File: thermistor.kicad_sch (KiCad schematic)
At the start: 2 parts, among them Q13 AO3400A

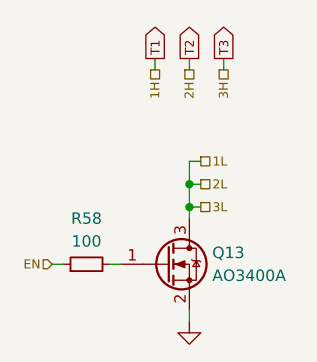
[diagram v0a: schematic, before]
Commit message: schematic: Reorder pages
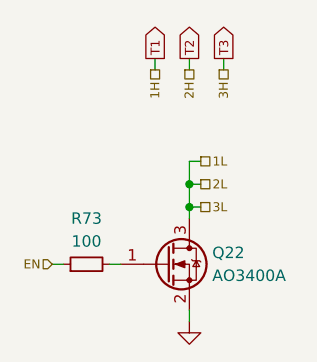
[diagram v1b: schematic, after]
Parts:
- renumbered Q13 to Q22, R58 to R73
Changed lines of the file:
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@@
 		(dnp no)
 		(fields_autoplaced yes)
-		(property "Reference" "R58"
+		(property "Reference" "R73"
 			(at 66.04 69.85 90)
 			(effects
@@
 		(on_board yes)
 		(dnp no)
-		(property "Reference" "Q13"
+		(property "Reference" "Q22"
 			(at 80.01 73.66 0)
 			(effects
@@
 		(dnp no)
 		(fields_autoplaced yes)
-		(property "Reference" "#PWR035"
+		(property "Reference" "#PWR063"
 			(at 77.47 87.63 0)
 			(effects

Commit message: schematic: Cleanup
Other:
- company: (none) -> York Formula Student
- title: (none) -> Battery Management System
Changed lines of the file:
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@@
 	(generator_version "8.0")
 	(paper "A4")
+	(title_block
+		(title "Battery Management System")
+		(date "2025-02-08")
+		(rev "1")
+		(company "York Formula Student")
+	)
 	(junction
 		(at 77.47 68.58)

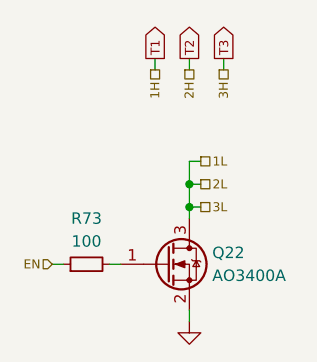
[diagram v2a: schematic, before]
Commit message: schematic: Re-annotate designators
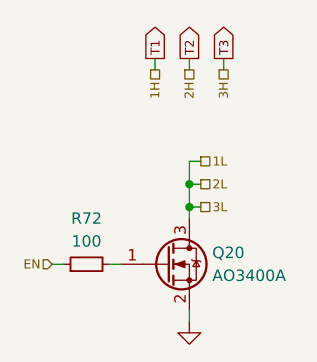
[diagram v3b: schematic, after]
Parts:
- renumbered Q22 to Q20, R73 to R72
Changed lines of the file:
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@@
 		(dnp no)
 		(fields_autoplaced yes)
-		(property "Reference" "R73"
+		(property "Reference" "R72"
 			(at 66.04 69.85 90)
 			(effects
@@
 			(project "bms"
 				(path "/ae4a7653-8e6d-4e05-b144-1e5e3b2092b7/22f96080-372f-4edc-adbb-6967cdfa7222/0d2d7204-129d-421c-bcc5-b71bb72cba95"
+					(reference "R72")
+					(unit 1)
+				)
+				(path "/ae4a7653-8e6d-4e05-b144-1e5e3b2092b7/22f96080-372f-4edc-adbb-6967cdfa7222/29137b06-2a79-41e8-a20a-ffb792999e98"
+					(reference "R74")
+					(unit 1)
+				)
+				(path "/ae4a7653-8e6d-4e05-b144-1e5e3b2092b7/22f96080-372f-4edc-adbb-6967cdfa7222/79ecc304-8e18-444c-9a27-bb0ae7f09105"
+					(reference "R71")
+					(unit 1)
+				)
+				(path "/ae4a7653-8e6d-4e05-b144-1e5e3b2092b7/22f96080-372f-4edc-adbb-6967cdfa7222/7d586639-e148-4a8a-9ad9-620c1fe14641"
+					(reference "R69")
+					(unit 1)
+				)
+				(path "/ae4a7653-8e6d-4e05-b144-1e5e3b2092b7/22f96080-372f-4edc-adbb-6967cdfa7222/8f54f16c-7967-437d-a988-e231275c63ab"
+					(reference "R66")
+					(unit 1)
+				)
+				(path "/ae4a7653-8e6d-4e05-b144-1e5e3b2092b7/22f96080-372f-4edc-adbb-6967cdfa7222/9c1ee688-8492-4d78-a310-31dcbd30b38f"
+					(reference "R68")
+					(unit 1)
+				)
+				(path "/ae4a7653-8e6d-4e05-b144-1e5e3b2092b7/22f96080-372f-4edc-adbb-6967cdfa7222/bb249f9a-39ea-44a6-9a0b-74cb85e10ca5"
+					(reference "R75")
+					(unit 1)
+				)
+				(path "/ae4a7653-8e6d-4e05-b144-1e5e3b2092b7/22f96080-372f-4edc-adbb-6967cdfa7222/efd357bc-4550-47fb-96bd-8f3dacb5f594"
 					(reference "R73")
 					(unit 1)
 				)
-				(path "/ae4a7653-8e6d-4e05-b144-1e5e3b2092b7/22f96080-372f-4edc-adbb-6967cdfa7222/29137b06-2a79-41e8-a20a-ffb792999e98"
-					(reference "R66")
-					(unit 1)
-				)
-				(path "/ae4a7653-8e6d-4e05-b144-1e5e3b2092b7/22f96080-372f-4edc-adbb-6967cdfa7222/79ecc304-8e18-444c-9a27-bb0ae7f09105"
-					(reference "R74")
-					(unit 1)
-				)
-				(path "/ae4a7653-8e6d-4e05-b144-1e5e3b2092b7/22f96080-372f-4edc-adbb-6967cdfa7222/7d586639-e148-4a8a-9ad9-620c1fe14641"
-					(reference "R68")
-					(unit 1)
-				)
-				(path "/ae4a7653-8e6d-4e05-b144-1e5e3b2092b7/22f96080-372f-4edc-adbb-6967cdfa7222/8f54f16c-7967-437d-a988-e231275c63ab"
-					(reference "R71")
-					(unit 1)
-				)
-				(path "/ae4a7653-8e6d-4e05-b144-1e5e3b2092b7/22f96080-372f-4edc-adbb-6967cdfa7222/9c1ee688-8492-4d78-a310-31dcbd30b38f"
-					(reference "R69")
-					(unit 1)
-				)
-				(path "/ae4a7653-8e6d-4e05-b144-1e5e3b2092b7/22f96080-372f-4edc-adbb-6967cdfa7222/bb249f9a-39ea-44a6-9a0b-74cb85e10ca5"
-					(reference "R63")
-					(unit 1)
-				)
-				(path "/ae4a7653-8e6d-4e05-b144-1e5e3b2092b7/22f96080-372f-4edc-adbb-6967cdfa7222/efd357bc-4550-47fb-96bd-8f3dacb5f594"
-					(reference "R72")
-					(unit 1)
-				)
 				(path "/ae4a7653-8e6d-4e05-b144-1e5e3b2092b7/22f96080-372f-4edc-adbb-6967cdfa7222/f122550a-f09a-4f05-9f89-cb0637def957"
-					(reference "R58")
+					(reference "R65")
 					(unit 1)
 				)
 				(path "/ae4a7653-8e6d-4e05-b144-1e5e3b2092b7/22f96080-372f-4edc-adbb-6967cdfa7222/fa4bad2a-a064-460b-8083-ff08c7505cb9"
+					(reference "R70")
+					(unit 1)
+				)
+				(path "/ae4a7653-8e6d-4e05-b144-1e5e3b2092b7/22f96080-372f-4edc-adbb-6967cdfa7222/fa95d462-4de0-4934-af70-5f0e8f1d034c"
 					(reference "R67")
-					(unit 1)
-				)
-				(path "/ae4a7653-8e6d-4e05-b144-1e5e3b2092b7/22f96080-372f-4edc-adbb-6967cdfa7222/fa95d462-4de0-4934-af70-5f0e8f1d034c"
-					(reference "R70")
 					(unit 1)
 				)
@@
 		(on_board yes)
 		(dnp no)
-		(property "Reference" "Q22"
+		(property "Reference" "Q20"
 			(at 80.01 73.66 0)
 			(effects
@@
 			(project "bms"
 				(path "/ae4a7653-8e6d-4e05-b144-1e5e3b2092b7/22f96080-372f-4edc-adbb-6967cdfa7222/0d2d7204-129d-421c-bcc5-b71bb72cba95"
+					(reference "Q20")
+					(unit 1)
+				)
+				(path "/ae4a7653-8e6d-4e05-b144-1e5e3b2092b7/22f96080-372f-4edc-adbb-6967cdfa7222/29137b06-2a79-41e8-a20a-ffb792999e98"
 					(reference "Q22")
 					(unit 1)
 				)
-				(path "/ae4a7653-8e6d-4e05-b144-1e5e3b2092b7/22f96080-372f-4edc-adbb-6967cdfa7222/29137b06-2a79-41e8-a20a-ffb792999e98"
-					(reference "Q15")
-					(unit 1)
-				)
 				(path "/ae4a7653-8e6d-4e05-b144-1e5e3b2092b7/22f96080-372f-4edc-adbb-6967cdfa7222/79ecc304-8e18-444c-9a27-bb0ae7f09105"
-					(reference "Q23")
+					(reference "Q19")
 					(unit 1)
 				)
@@
 				)
 				(path "/ae4a7653-8e6d-4e05-b144-1e5e3b2092b7/22f96080-372f-4edc-adbb-6967cdfa7222/8f54f16c-7967-437d-a988-e231275c63ab"
-					(reference "Q20")
+					(reference "Q14")
 					(unit 1)
 				)
 				(path "/ae4a7653-8e6d-4e05-b144-1e5e3b2092b7/22f96080-372f-4edc-adbb-6967cdfa7222/9c1ee688-8492-4d78-a310-31dcbd30b38f"
-					(reference "Q18")
+					(reference "Q16")
 					(unit 1)
 				)
 				(path "/ae4a7653-8e6d-4e05-b144-1e5e3b2092b7/22f96080-372f-4edc-adbb-6967cdfa7222/bb249f9a-39ea-44a6-9a0b-74cb85e10ca5"
-					(reference "Q14")
+					(reference "Q23")
 					(unit 1)
 				)
@@
 				)
 				(path "/ae4a7653-8e6d-4e05-b144-1e5e3b2092b7/22f96080-372f-4edc-adbb-6967cdfa7222/fa4bad2a-a064-460b-8083-ff08c7505cb9"
-					(reference "Q16")
+					(reference "Q18")
 					(unit 1)
 				)
 				(path "/ae4a7653-8e6d-4e05-b144-1e5e3b2092b7/22f96080-372f-4edc-adbb-6967cdfa7222/fa95d462-4de0-4934-af70-5f0e8f1d034c"
-					(reference "Q19")
+					(reference "Q15")
 					(unit 1)
 				)
@@
 		(dnp no)
 		(fields_autoplaced yes)
-		(property "Reference" "#PWR063"
+		(property "Reference" "#PWR064"
 			(at 77.47 87.63 0)
 			(effects
@@
 			(project "bms"
 				(path "/ae4a7653-8e6d-4e05-b144-1e5e3b2092b7/22f96080-372f-4edc-adbb-6967cdfa7222/0d2d7204-129d-421c-bcc5-b71bb72cba95"
+					(reference "#PWR064")
+					(unit 1)
+				)
+				(path "/ae4a7653-8e6d-4e05-b144-1e5e3b2092b7/22f96080-372f-4edc-adbb-6967cdfa7222/29137b06-2a79-41e8-a20a-ffb792999e98"
+					(reference "#PWR066")
+					(unit 1)
+				)
+				(path "/ae4a7653-8e6d-4e05-b144-1e5e3b2092b7/22f96080-372f-4edc-adbb-6967cdfa7222/79ecc304-8e18-444c-9a27-bb0ae7f09105"
 					(reference "#PWR063")
 					(unit 1)
 				)
-				(path "/ae4a7653-8e6d-4e05-b144-1e5e3b2092b7/22f96080-372f-4edc-adbb-6967cdfa7222/29137b06-2a79-41e8-a20a-ffb792999e98"
-					(reference "#PWR056")
-					(unit 1)
-				)
-				(path "/ae4a7653-8e6d-4e05-b144-1e5e3b2092b7/22f96080-372f-4edc-adbb-6967cdfa7222/79ecc304-8e18-444c-9a27-bb0ae7f09105"
-					(reference "#PWR064")
-					(unit 1)
-				)
 				(path "/ae4a7653-8e6d-4e05-b144-1e5e3b2092b7/22f96080-372f-4edc-adbb-6967cdfa7222/7d586639-e148-4a8a-9ad9-620c1fe14641"
+					(reference "#PWR061")
+					(unit 1)
+				)
+				(path "/ae4a7653-8e6d-4e05-b144-1e5e3b2092b7/22f96080-372f-4edc-adbb-6967cdfa7222/8f54f16c-7967-437d-a988-e231275c63ab"
 					(reference "#PWR058")
 					(unit 1)
 				)
-				(path "/ae4a7653-8e6d-4e05-b144-1e5e3b2092b7/22f96080-372f-4edc-adbb-6967cdfa7222/8f54f16c-7967-437d-a988-e231275c63ab"
-					(reference "#PWR061")
-					(unit 1)
-				)
 				(path "/ae4a7653-8e6d-4e05-b144-1e5e3b2092b7/22f96080-372f-4edc-adbb-6967cdfa7222/9c1ee688-8492-4d78-a310-31dcbd30b38f"
+					(reference "#PWR060")
+					(unit 1)
+				)
+				(path "/ae4a7653-8e6d-4e05-b144-1e5e3b2092b7/22f96080-372f-4edc-adbb-6967cdfa7222/bb249f9a-39ea-44a6-9a0b-74cb85e10ca5"
+					(reference "#PWR067")
+					(unit 1)
+				)
+				(path "/ae4a7653-8e6d-4e05-b144-1e5e3b2092b7/22f96080-372f-4edc-adbb-6967cdfa7222/efd357bc-4550-47fb-96bd-8f3dacb5f594"
+					(reference "#PWR065")
+					(unit 1)
+				)
+				(path "/ae4a7653-8e6d-4e05-b144-1e5e3b2092b7/22f96080-372f-4edc-adbb-6967cdfa7222/f122550a-f09a-4f05-9f89-cb0637def957"
+					(reference "#PWR057")
+					(unit 1)
+				)
+				(path "/ae4a7653-8e6d-4e05-b144-1e5e3b2092b7/22f96080-372f-4edc-adbb-6967cdfa7222/fa4bad2a-a064-460b-8083-ff08c7505cb9"
+					(reference "#PWR062")
+					(unit 1)
+				)
+				(path "/ae4a7653-8e6d-4e05-b144-1e5e3b2092b7/22f96080-372f-4edc-adbb-6967cdfa7222/fa95d462-4de0-4934-af70-5f0e8f1d034c"
 					(reference "#PWR059")
 					(unit 1)
 				)
-				(path "/ae4a7653-8e6d-4e05-b144-1e5e3b2092b7/22f96080-372f-4edc-adbb-6967cdfa7222/bb249f9a-39ea-44a6-9a0b-74cb85e10ca5"
-					(reference "#PWR055")
-					(unit 1)
-				)
-				(path "/ae4a7653-8e6d-4e05-b144-1e5e3b2092b7/22f96080-372f-4edc-adbb-6967cdfa7222/efd357bc-4550-47fb-96bd-8f3dacb5f594"
-					(reference "#PWR062")
-					(unit 1)
-				)
-				(path "/ae4a7653-8e6d-4e05-b144-1e5e3b2092b7/22f96080-372f-4edc-adbb-6967cdfa7222/f122550a-f09a-4f05-9f89-cb0637def957"
-					(reference "#PWR035")
-					(unit 1)
-				)
-				(path "/ae4a7653-8e6d-4e05-b144-1e5e3b2092b7/22f96080-372f-4edc-adbb-6967cdfa7222/fa4bad2a-a064-460b-8083-ff08c7505cb9"
-					(reference "#PWR057")
-					(unit 1)
-				)
-				(path "/ae4a7653-8e6d-4e05-b144-1e5e3b2092b7/22f96080-372f-4edc-adbb-6967cdfa7222/fa95d462-4de0-4934-af70-5f0e8f1d034c"
-					(reference "#PWR060")
-					(unit 1)
-				)

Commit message: schematic: Don't make CV12 go through fuse and adjust thermistor pinout
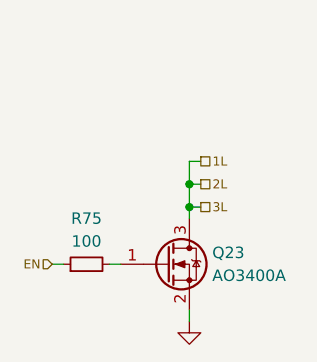
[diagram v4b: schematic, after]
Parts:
- renumbered Q20 to Q23, R72 to R75

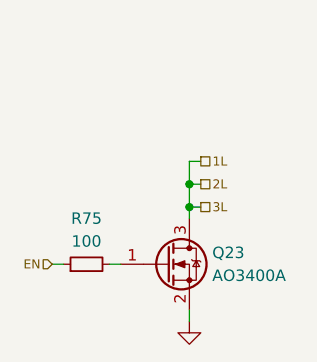
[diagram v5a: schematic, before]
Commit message: schematic: Cleanup BOM
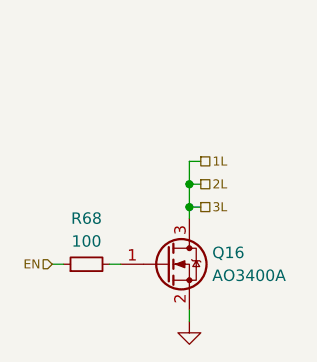
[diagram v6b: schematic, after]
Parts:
- Q16: renamed from Q23; Dist (none) -> LCSC; Dist # (none) -> C347475; Mfr (none) -> UMW; Mfr # (none) -> AO3400A; Role Balance MOSFET -> (none)
- R68: renamed from R75; Dist (none) -> LCSC; Dist # (none) -> C22775; Mfr (none) -> Uni-Royal; Mfr # (none) -> 0603WAF1000T5E; Role Thermistor MOSFET gate resistor -> (none)
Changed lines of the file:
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@@
 		(dnp no)
 		(fields_autoplaced yes)
-		(property "Reference" "R75"
+		(property "Reference" "R68"
 			(at 66.04 69.85 90)
 			(effects
@@
 			)
 		)
-		(property "Role" "Thermistor MOSFET gate resistor"
+		(property "Dist #" "C22775"
+			(at 66.04 74.93 0)
+			(effects
+				(font
+					(size 1.27 1.27)
+				)
+				(hide yes)
+			)
+		)
+		(property "Mfr" "Uni-Royal"
+			(at 66.04 74.93 0)
+			(effects
+				(font
+					(size 1.27 1.27)
+				)
+				(hide yes)
+			)
+		)
+		(property "Mfr #" "0603WAF1000T5E"
+			(at 66.04 74.93 0)
+			(effects
+				(font
+					(size 1.27 1.27)
+				)
+				(hide yes)
+			)
+		)
+		(property "Dist" "LCSC"
 			(at 66.04 74.93 0)
 			(effects
@@
 		(on_board yes)
 		(dnp no)
-		(property "Reference" "Q23"
+		(property "Reference" "Q16"
 			(at 80.01 73.66 0)
 			(effects
@@
 			)
 		)
-		(property "Role" "Balance MOSFET"
+		(property "Dist #" "C347475"
+			(at 74.93 74.93 0)
+			(effects
+				(font
+					(size 1.27 1.27)
+				)
+				(hide yes)
+			)
+		)
+		(property "Mfr" "UMW"
+			(at 74.93 74.93 0)
+			(effects
+				(font
+					(size 1.27 1.27)
+				)
+				(hide yes)
+			)
+		)
+		(property "Mfr #" "AO3400A"
+			(at 74.93 74.93 0)
+			(effects
+				(font
+					(size 1.27 1.27)
+				)
+				(hide yes)
+			)
+		)
+		(property "Dist" "LCSC"
 			(at 74.93 74.93 0)
 			(effects
@@
 		(dnp no)
 		(fields_autoplaced yes)
-		(property "Reference" "#PWR065"
+		(property "Reference" "#PWR09"
 			(at 77.47 87.63 0)
 			(effects

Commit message: *: Update to kicad 9.0.0
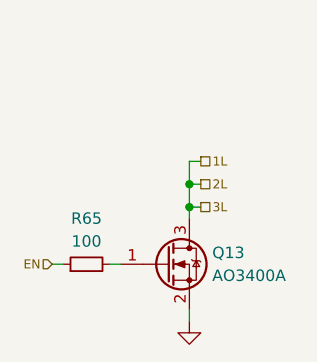
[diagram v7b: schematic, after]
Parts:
- renumbered Q16 to Q13, R68 to R65
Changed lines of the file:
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@@
 (kicad_sch
-	(version 20231120)
+	(version 20250114)
 	(generator "eeschema")
-	(generator_version "8.0")
+	(generator_version "9.0")
 	(paper "A4")
 	(title_block
@@
 		(dnp no)
 		(fields_autoplaced yes)
-		(property "Reference" "R68"
+		(property "Reference" "R65"
 			(at 66.04 69.85 90)
 			(effects
@@
 		(on_board yes)
 		(dnp no)
-		(property "Reference" "Q16"
+		(property "Reference" "Q13"
 			(at 80.01 73.66 0)
 			(effects
@@
 		(dnp no)
 		(fields_autoplaced yes)
-		(property "Reference" "#PWR09"
+		(property "Reference" "#PWR057"
 			(at 77.47 87.63 0)
 			(effects
